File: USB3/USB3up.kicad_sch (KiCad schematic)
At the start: 2 parts

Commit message: usb3 work cont
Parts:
- added C23: 10uF, symbol Device:C
- added R22, R23: 90.9k, symbol Device:R
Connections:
- net GND: now also C23.1, R23.2
- net USB_VBUS: now also R22.2, R23.1
- new net VCC5V0_USB3: C23.2, R22.1

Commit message: usb3 work cont
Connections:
- net USB_VBUS: no longer names the net of R22.2, R23.1
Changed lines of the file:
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@@
-		)
-	)
-	(global_label "USB_SSRXM_UP"
-		(shape input)
-		(at 217.17 59.69 0)
-		(fields_autoplaced yes)
-		(effects
-			(font
-				(size 1.27 1.27)
-			)
-			(justify left)
-		)
-		(property "Intersheetrefs" "${INTERSHEET_REFS}"
-			(at 234.8508 59.69 0)
-			(effects
-				(font
-					(size 1.27 1.27)
-				)
-				(justify left)
-				(hide yes)
-			)
-		)
-	)
-	(global_label "USB_DM_UP"
-		(shape input)
-		(at 217.17 44.45 0)
-		(fields_autoplaced yes)
-		(effects
-			(font
-				(size 1.27 1.27)
-			)
-			(justify left)
-		)
-		(property "Intersheetrefs" "${INTERSHEET_REFS}"
-			(at 231.2223 44.45 0)
-			(effects
-				(font
-					(size 1.27 1.27)
-				)
-				(justify left)
-				(hide yes)
-			)
-		)
-	)
-	(global_label "USB_SSTXM_UP"
-		(shape input)
-		(at 217.17 52.07 0)
-		(fields_autoplaced yes)
-		(effects
-			(font
-				(size 1.27 1.27)
-			)
-			(justify left)
-		)
-		(property "Intersheetrefs" "${INTERSHEET_REFS}"
-			(at 234.5484 52.07 0)
-			(effects
-				(font
-					(size 1.27 1.27)
-				)
-				(justify left)
-				(hide yes)
-			)
 		)
 	)
@@
 				(hide yes)
 			)
-		)
-	)
-	(global_label "USB_SSRXP_UP"
-		(shape input)
-		(at 217.17 62.23 0)
-		(fields_autoplaced yes)
-		(effects
-			(font
-				(size 1.27 1.27)
-			)
-			(justify left)
-		)
-		(property "Intersheetrefs" "${INTERSHEET_REFS}"
-			(at 234.6694 62.23 0)
-			(effects
-				(font
-					(size 1.27 1.27)
-				)
-				(justify left)
-				(hide yes)
-			)
-		)
-	)
-	(global_label "USB_SSTXP_UP"
-		(shape input)
-		(at 217.17 54.61 0)
-		(fields_autoplaced yes)
-		(effects
-			(font
-				(size 1.27 1.27)
-			)
-			(justify left)
-		)
-		(property "Intersheetrefs" "${INTERSHEET_REFS}"
-			(at 234.367 54.61 0)
-			(effects
-				(font
-					(size 1.27 1.27)
-				)
-				(justify left)
-				(hide yes)
-			)
-		)
-	)
-	(global_label "USB_VBUS"
-		(shape input)
-		(at 217.17 38.1 0)
-		(fields_autoplaced yes)
-		(effects
-			(font
-				(size 1.27 1.27)
-			)
-			(justify left)
-		)
-		(property "Intersheetrefs" "${INTERSHEET_REFS}"
-			(at 229.8314 38.1 0)
-			(effects
-				(font
-					(size 1.27 1.27)
-				)
-				(justify left)
-				(hide yes)
-			)
-		)
-	)
-	(global_label "USB_DP_UP"
-		(shape input)
-		(at 217.17 46.99 0)
-		(fields_autoplaced yes)
-		(effects
-			(font
-				(size 1.27 1.27)
-			)
-			(justify left)
-		)
-		(property "Intersheetrefs" "${INTERSHEET_REFS}"
-			(at 231.0409 46.99 0)
-			(effects
-				(font
-					(size 1.27 1.27)
-				)
-				(justify left)
-				(hide yes)
-			)

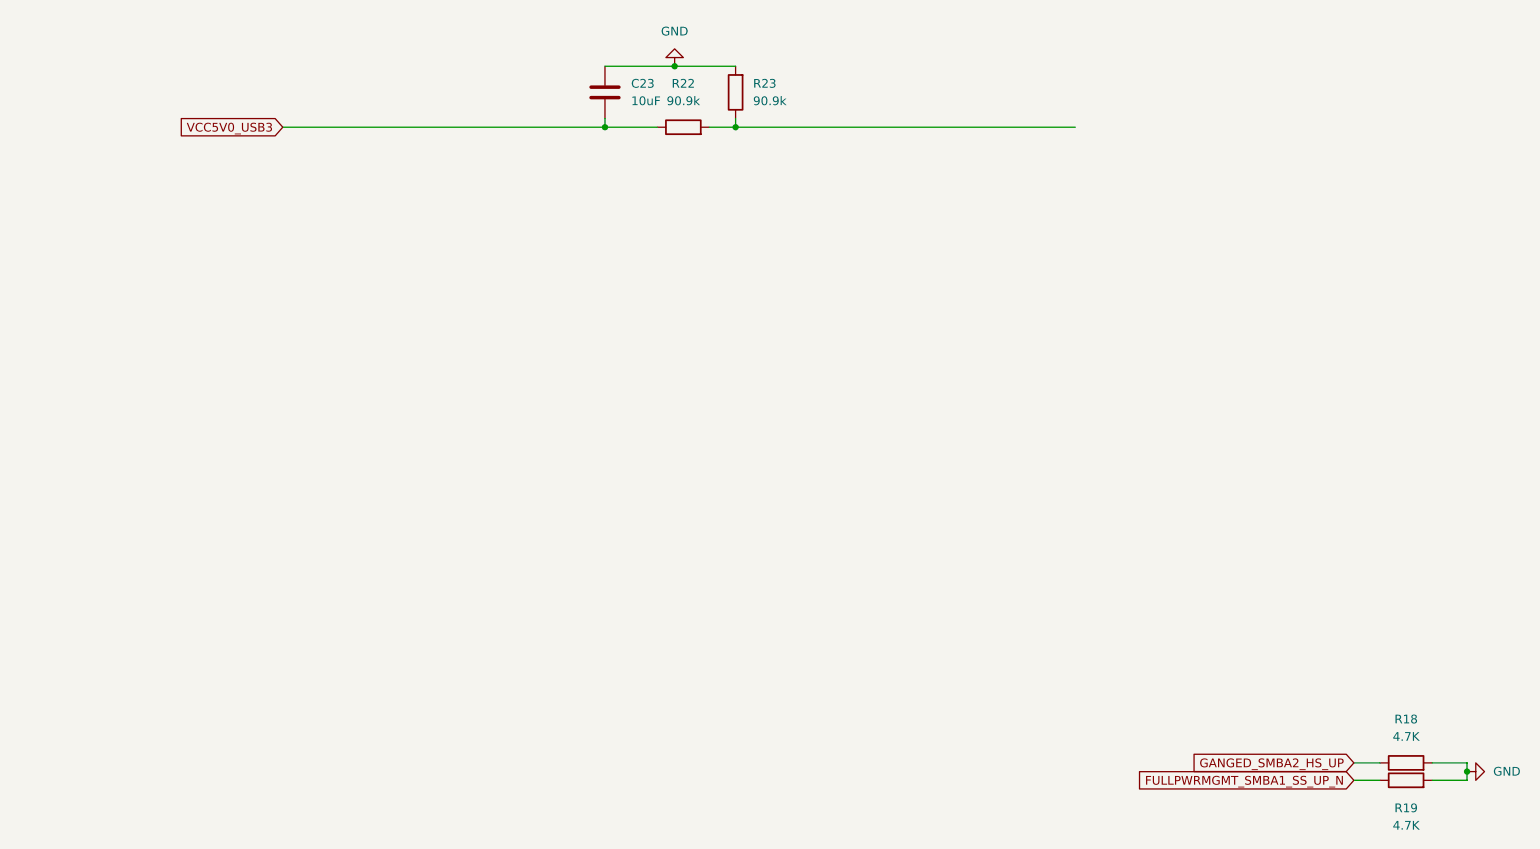
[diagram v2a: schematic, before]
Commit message: usb3up done, usb3down begun
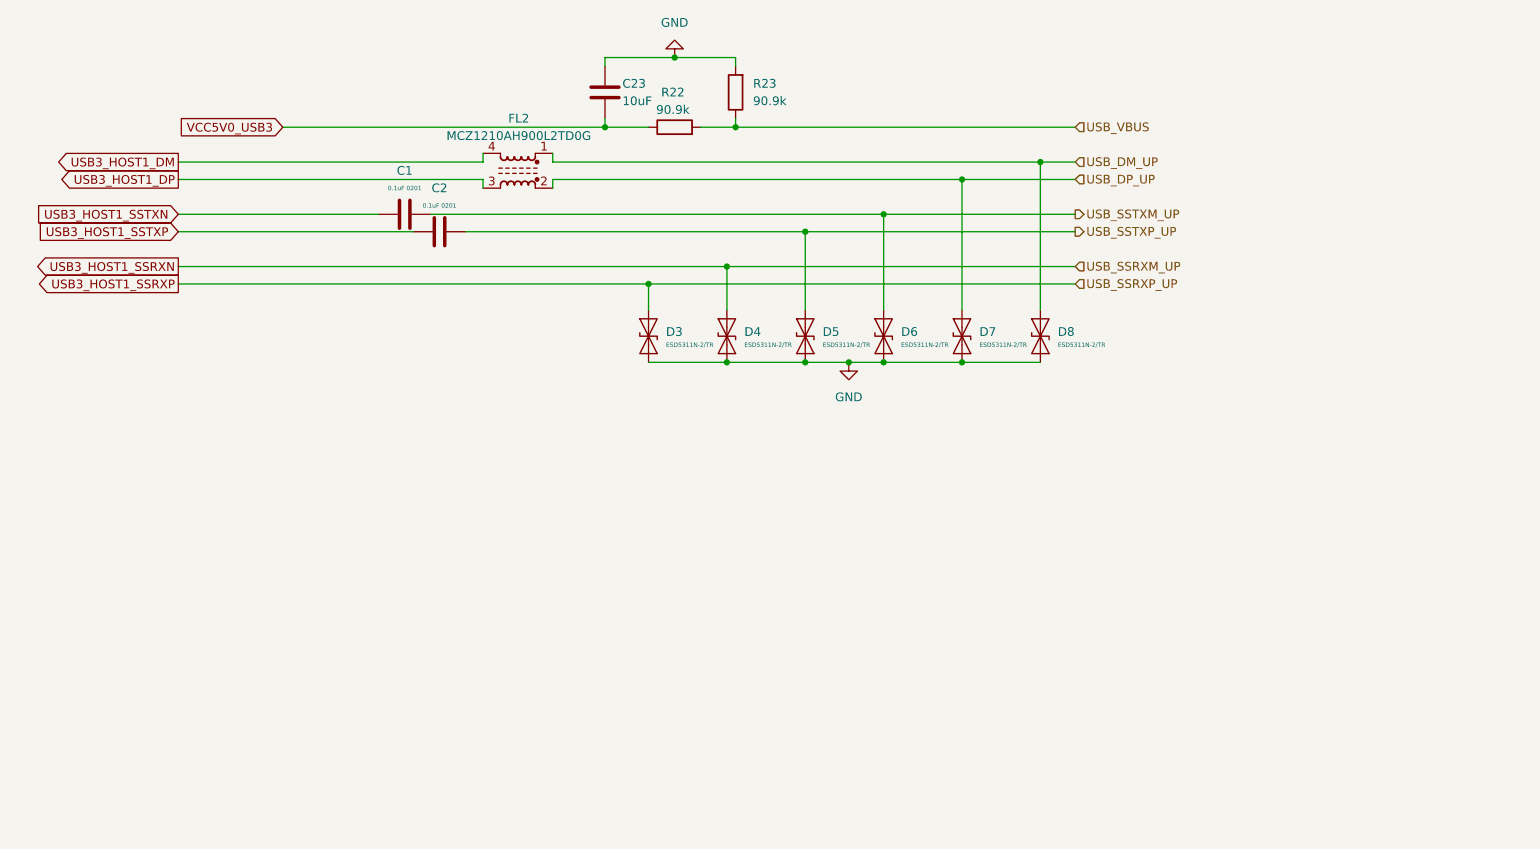
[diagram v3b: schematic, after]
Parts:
- removed R18, R19: 4.7K, symbol Device:R
- added C1, C2: 0.1uF 0201, symbol Device:C
- added D3, D4, D5, D6, D7, D8: ESD5311N-2/TR, Diode_SMD:Infineon_SG-WLL-2-3_0.58x0.28_P0.36mm, symbol Diode:ESD131-B1-W0201
- added FL2: MCZ1210AH900L2TD0G, symbol Filter:Choke_CommonMode_FerriteCore_1423
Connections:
- net GND: now also D3.2 (A2), D4.2 (A2), D5.2 (A2), D6.2 (A2), D7.2 (A2), D8.2 (A2)
- net USB_VBUS: now reaches R22.2, R23.1
- new net USB3_HOST1_DM: FL2.4
- new net USB3_HOST1_DP: FL2.3
- new net USB3_HOST1_SSRXN: D4.1 (A1)
- new net USB3_HOST1_SSRXP: D3.1 (A1)
- new net USB3_HOST1_SSTXN: C1.1
- new net USB3_HOST1_SSTXP: C2.1
- new net USB_DM_UP: D8.1 (A1), FL2.1
- new net USB_DP_UP: D7.1 (A1), FL2.2
- new net USB_SSTXM_UP: C1.2, D6.1 (A1)
- new net USB_SSTXP_UP: C2.2, D5.1 (A1)
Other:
- moved on the sheet: R22

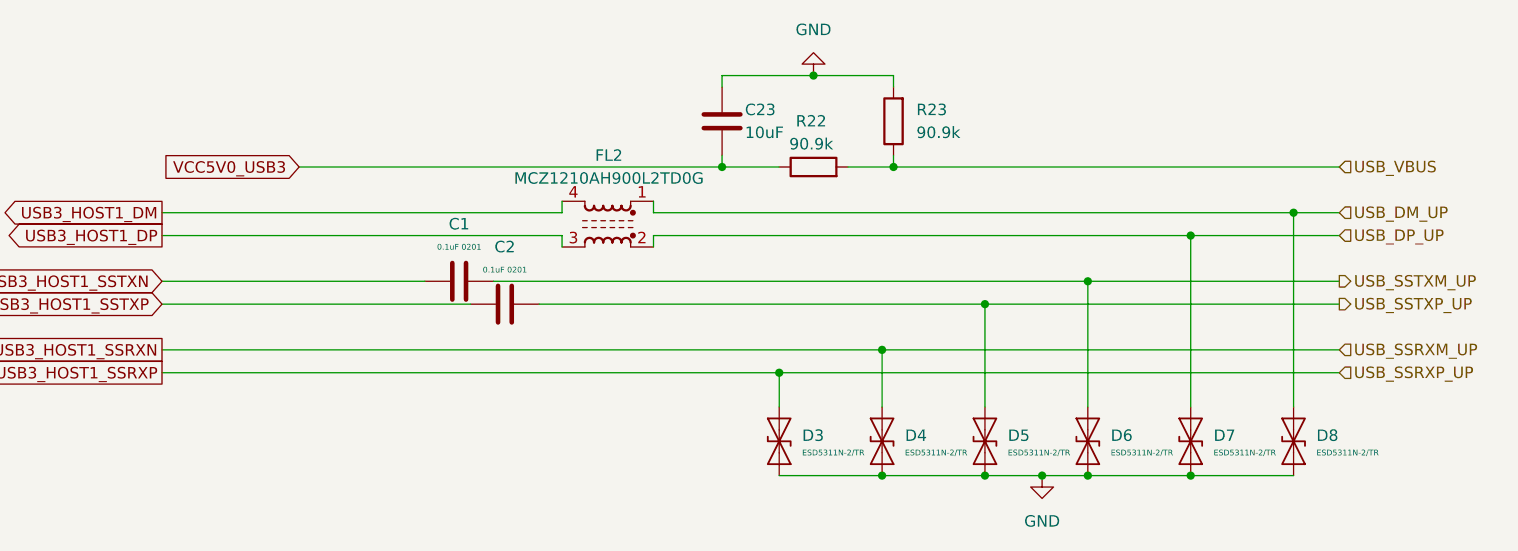
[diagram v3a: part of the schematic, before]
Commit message: usb3 down done
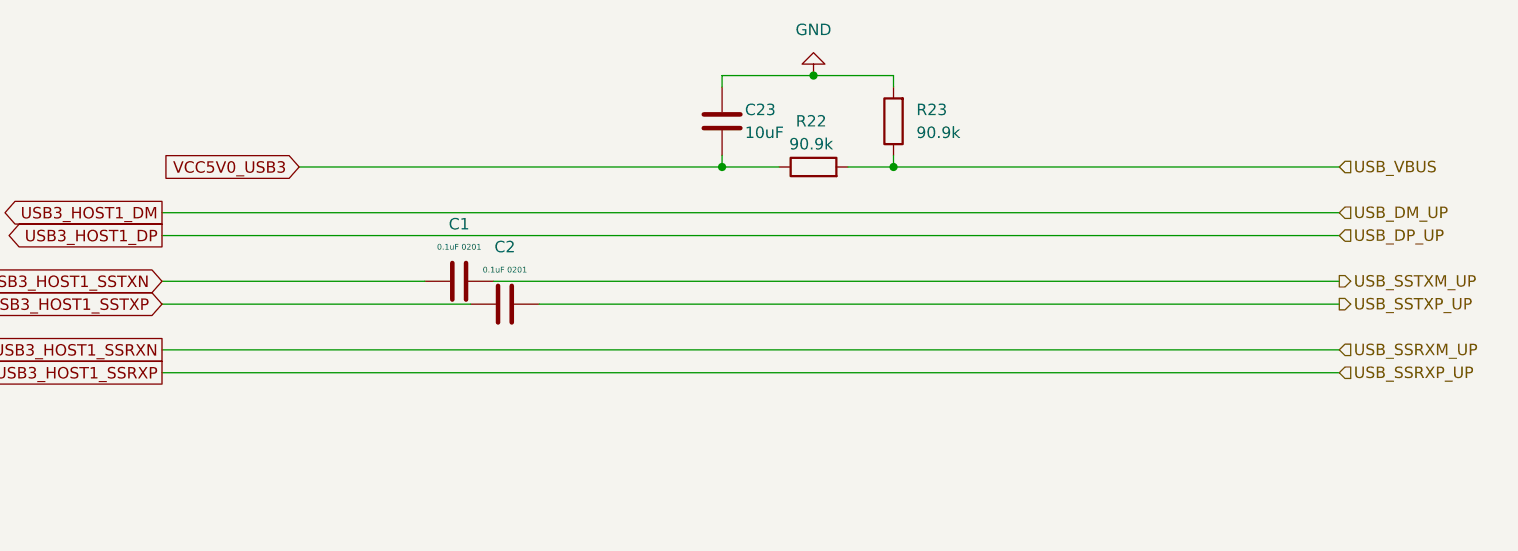
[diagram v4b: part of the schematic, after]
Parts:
- removed D3, D4, D5, D6, D7, D8: ESD5311N-2/TR, Diode_SMD:Infineon_SG-WLL-2-3_0.58x0.28_P0.36mm, symbol Diode:ESD131-B1-W0201
- removed FL2: MCZ1210AH900L2TD0G, symbol Filter:Choke_CommonMode_FerriteCore_1423

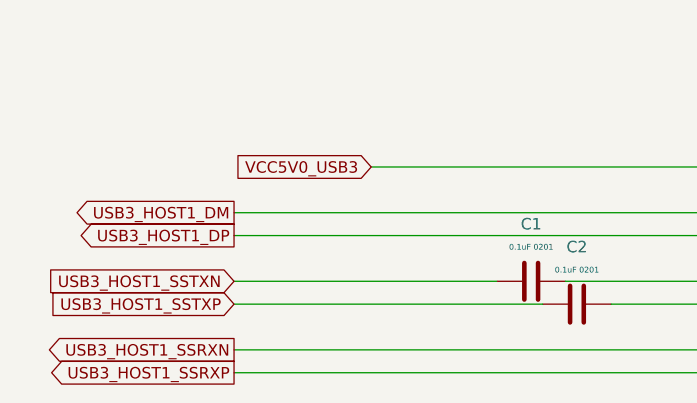
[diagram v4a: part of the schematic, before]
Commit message: finished usb3.0
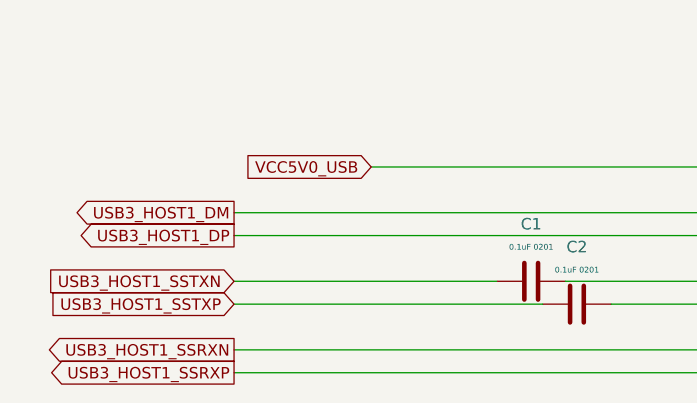
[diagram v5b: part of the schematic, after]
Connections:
- net VCC5V0_USB3 renamed VCC5V0_USB
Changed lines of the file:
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@@
+		)
+	)
+	(global_label "VCC5V0_USB"
+		(shape input)
+		(at 101.6 38.1 180)
+		(fields_autoplaced yes)
+		(effects
+			(font
+				(size 1.27 1.27)
+			)
+			(justify right)
+		)
+		(property "Intersheetrefs" "${INTERSHEET_REFS}"
+			(at 86.701 38.1 0)
+			(effects
+				(font
+					(size 1.27 1.27)
+				)
+				(justify right)
+				(hide yes)
+			)
 		)
 	)
@@
 				(hide yes)
 			)
-		)
-	)
-	(global_label "VCC5V0_USB3"
-		(shape input)
-		(at 101.6 38.1 180)
-		(fields_autoplaced yes)
-		(effects
-			(font
-				(size 1.27 1.27)
-			)
-			(justify right)
-		)
-		(property "Intersheetrefs" "${INTERSHEET_REFS}"
-			(at 85.4915 38.1 0)
-			(effects
-				(font
-					(size 1.27 1.27)
-				)
-				(justify right)
-				(hide yes)
-			)
